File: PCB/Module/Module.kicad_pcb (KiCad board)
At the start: 2 copper layers, 37.6 x 37.6 mm, 30 parts, among them J1 SWD_Programmer, J2 Conn_01x01, J3 Conn_01x01, J4 Conn_01x01, J5 Conn_01x01, U1 PY32F002BF15P6TU, U6 HallLinearSensor

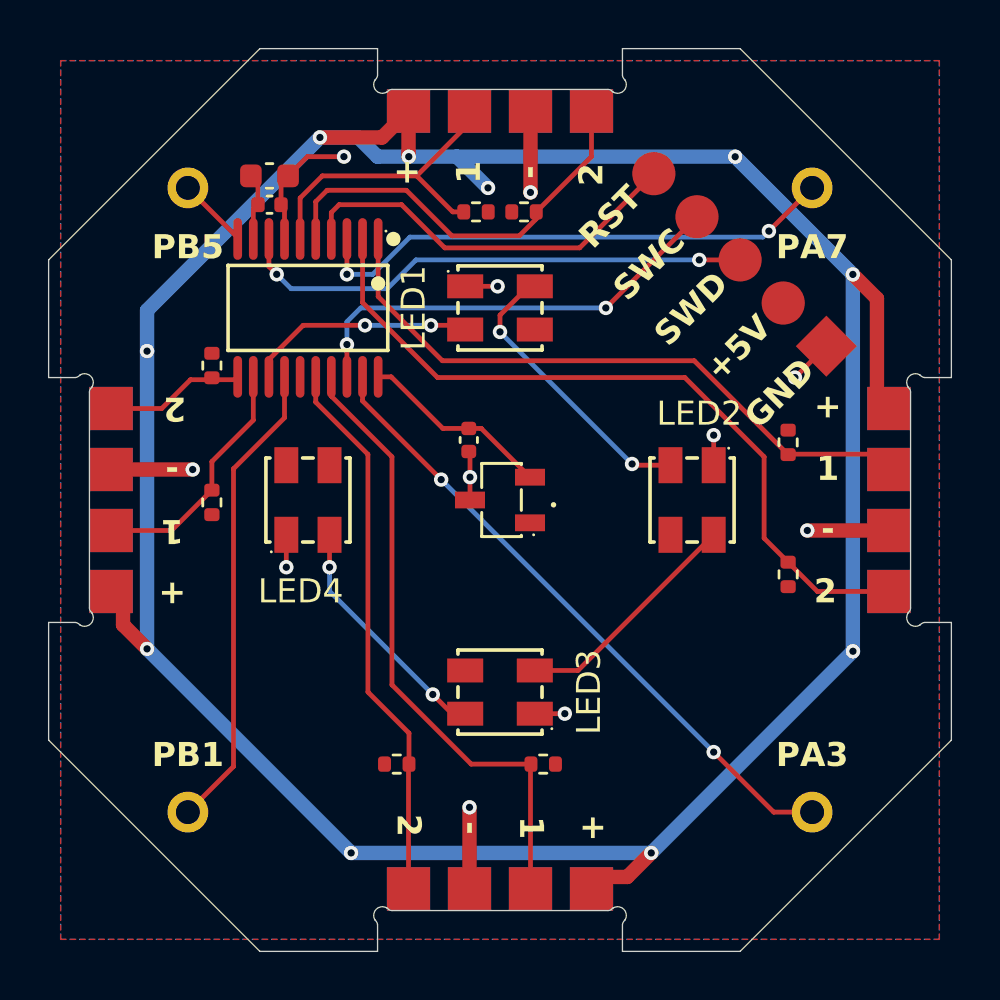
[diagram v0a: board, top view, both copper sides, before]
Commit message: Add electrolytic bulk capacitors to modules and power supply
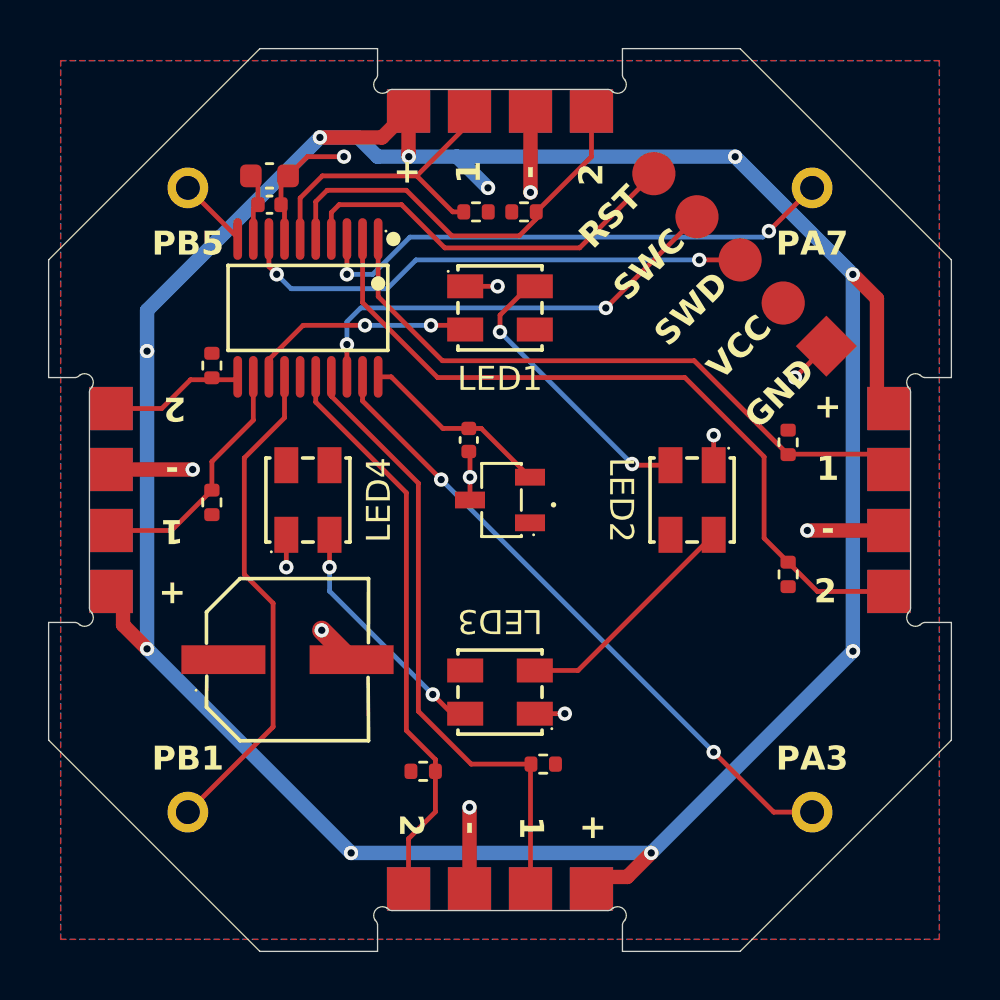
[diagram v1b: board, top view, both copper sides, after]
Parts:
- added C4: 470uF Electrolytic, CustomFootprints:CAP-SMD_BD6.3-L6.6-W6.6-FD, F.Cu at (141.2, 106.7)
- moved R5 1.14 mm to (146.8, 111.3)
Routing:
- net GND: track 28.1 -> 29.9 mm, vias 11 -> 12
- net /ShieldBottomLeft: track 19.8 -> 20.8 mm
- net /DataBottom2: track 22.9 -> 23.9 mm
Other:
- board text added: "VCC"
- board text removed: "+5V"
